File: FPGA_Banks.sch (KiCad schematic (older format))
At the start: 36 parts

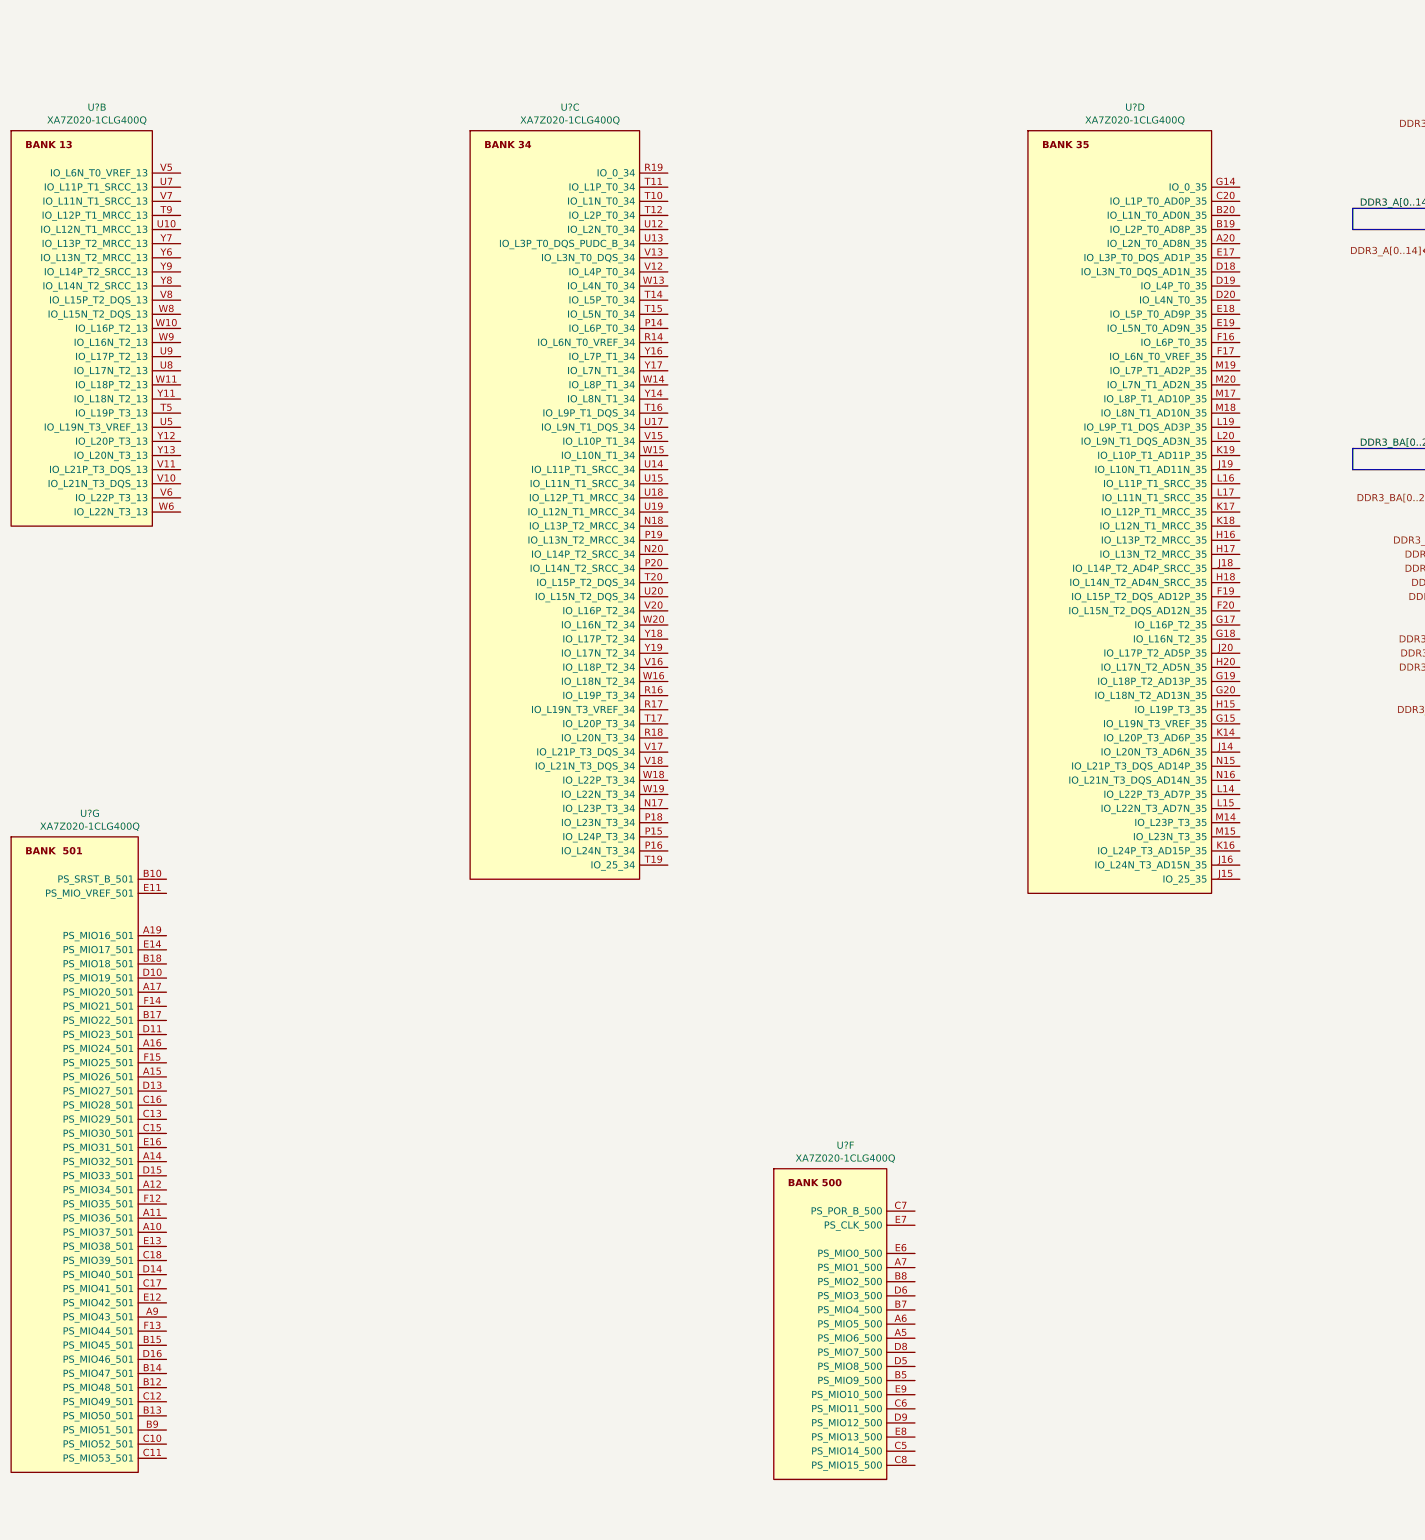
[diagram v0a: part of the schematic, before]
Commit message: Rearranged the top sheet blocks modified hir. pins in few blocks
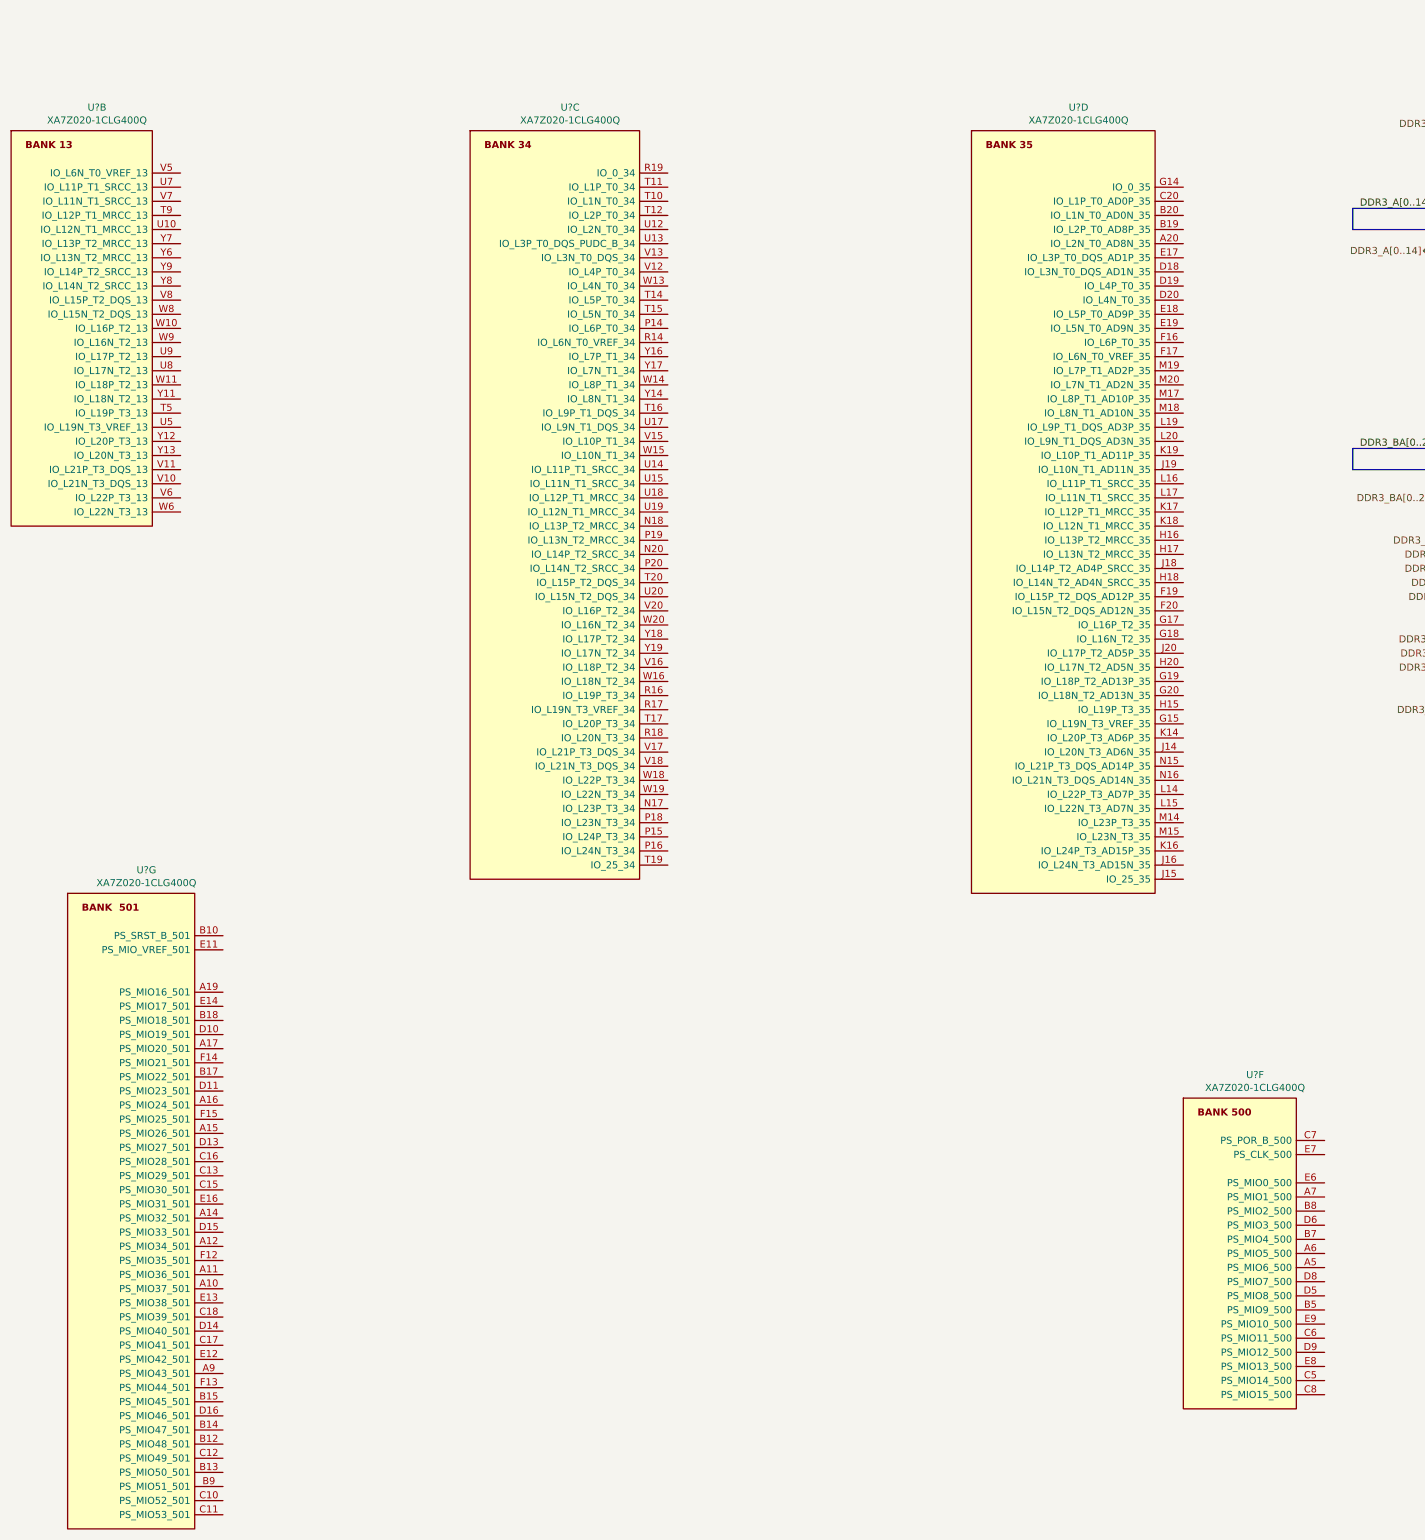
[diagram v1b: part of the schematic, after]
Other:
- moved on the sheet: U?D, U?F, U?G
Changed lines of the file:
@@
 L GM_FPGA:XA7Z020-1CLG400Q U?
 U 4 1 604A2214
-P 8200 1100
-F 0 "U?" H 8958 1265 50  0000 C CNN
-F 1 "XA7Z020-1CLG400Q" H 8958 1174 50  0000 C CNN
-F 2 "BGA400C80P20X20_1700X1700X160" H 11050 1200 50  0001 L CNN
-F 3 "http://www.xilinx.com/support/documentation/data_sheets/ds188-XA-Zynq-7000-Overview.pdf" H 11050 1100 50  0001 L CNN
-F 4 "XA7Z020-1CLG400Q" H 8200 1100 50  0001 C CNN "MPN"
-	4    8200 1100
+P 7800 1100
+F 0 "U?" H 8558 1265 50  0000 C CNN
+F 1 "XA7Z020-1CLG400Q" H 8558 1174 50  0000 C CNN
+F 2 "BGA400C80P20X20_1700X1700X160" H 10650 1200 50  0001 L CNN
+F 3 "http://www.xilinx.com/support/documentation/data_sheets/ds188-XA-Zynq-7000-Overview.pdf" H 10650 1100 50  0001 L CNN
+F 4 "XA7Z020-1CLG400Q" H 7800 1100 50  0001 C CNN "MPN"
+	4    7800 1100
 	1    0    0    -1
 $EndComp
@@
 L GM_FPGA:XA7Z020-1CLG400Q U?
 U 6 1 604B00A9
-P 6400 8450
-F 0 "U?" H 6908 8615 50  0000 C CNN
-F 1 "XA7Z020-1CLG400Q" H 6908 8524 50  0000 C CNN
-F 2 "BGA400C80P20X20_1700X1700X160" H 9250 8550 50  0001 L CNN
-F 3 "http://www.xilinx.com/support/documentation/data_sheets/ds188-XA-Zynq-7000-Overview.pdf" H 9250 8450 50  0001 L CNN
-F 4 "XA7Z020-1CLG400Q" H 6400 8450 50  0001 C CNN "MPN"
-	6    6400 8450
+P 9300 7950
+F 0 "U?" H 9808 8115 50  0000 C CNN
+F 1 "XA7Z020-1CLG400Q" H 9808 8024 50  0000 C CNN
+F 2 "BGA400C80P20X20_1700X1700X160" H 12150 8050 50  0001 L CNN
+F 3 "http://www.xilinx.com/support/documentation/data_sheets/ds188-XA-Zynq-7000-Overview.pdf" H 12150 7950 50  0001 L CNN
+F 4 "XA7Z020-1CLG400Q" H 9300 7950 50  0001 C CNN "MPN"
+	6    9300 7950
 	1    0    0    -1
 $EndComp
@@
 L GM_FPGA:XA7Z020-1CLG400Q U?
 U 7 1 604BC2A9
-P 1000 6100
-F 0 "U?" H 1558 6265 50  0000 C CNN
-F 1 "XA7Z020-1CLG400Q" H 1558 6174 50  0000 C CNN
-F 2 "BGA400C80P20X20_1700X1700X160" H 3850 6200 50  0001 L CNN
-F 3 "http://www.xilinx.com/support/documentation/data_sheets/ds188-XA-Zynq-7000-Overview.pdf" H 3850 6100 50  0001 L CNN
-F 4 "XA7Z020-1CLG400Q" H 1000 6100 50  0001 C CNN "MPN"
-	7    1000 6100
+P 1400 6500
+F 0 "U?" H 1958 6665 50  0000 C CNN
+F 1 "XA7Z020-1CLG400Q" H 1958 6574 50  0000 C CNN
+F 2 "BGA400C80P20X20_1700X1700X160" H 4250 6600 50  0001 L CNN
+F 3 "http://www.xilinx.com/support/documentation/data_sheets/ds188-XA-Zynq-7000-Overview.pdf" H 4250 6500 50  0001 L CNN
+F 4 "XA7Z020-1CLG400Q" H 1400 6500 50  0001 C CNN "MPN"
+	7    1400 6500
 	1    0    0    -1
 $EndComp

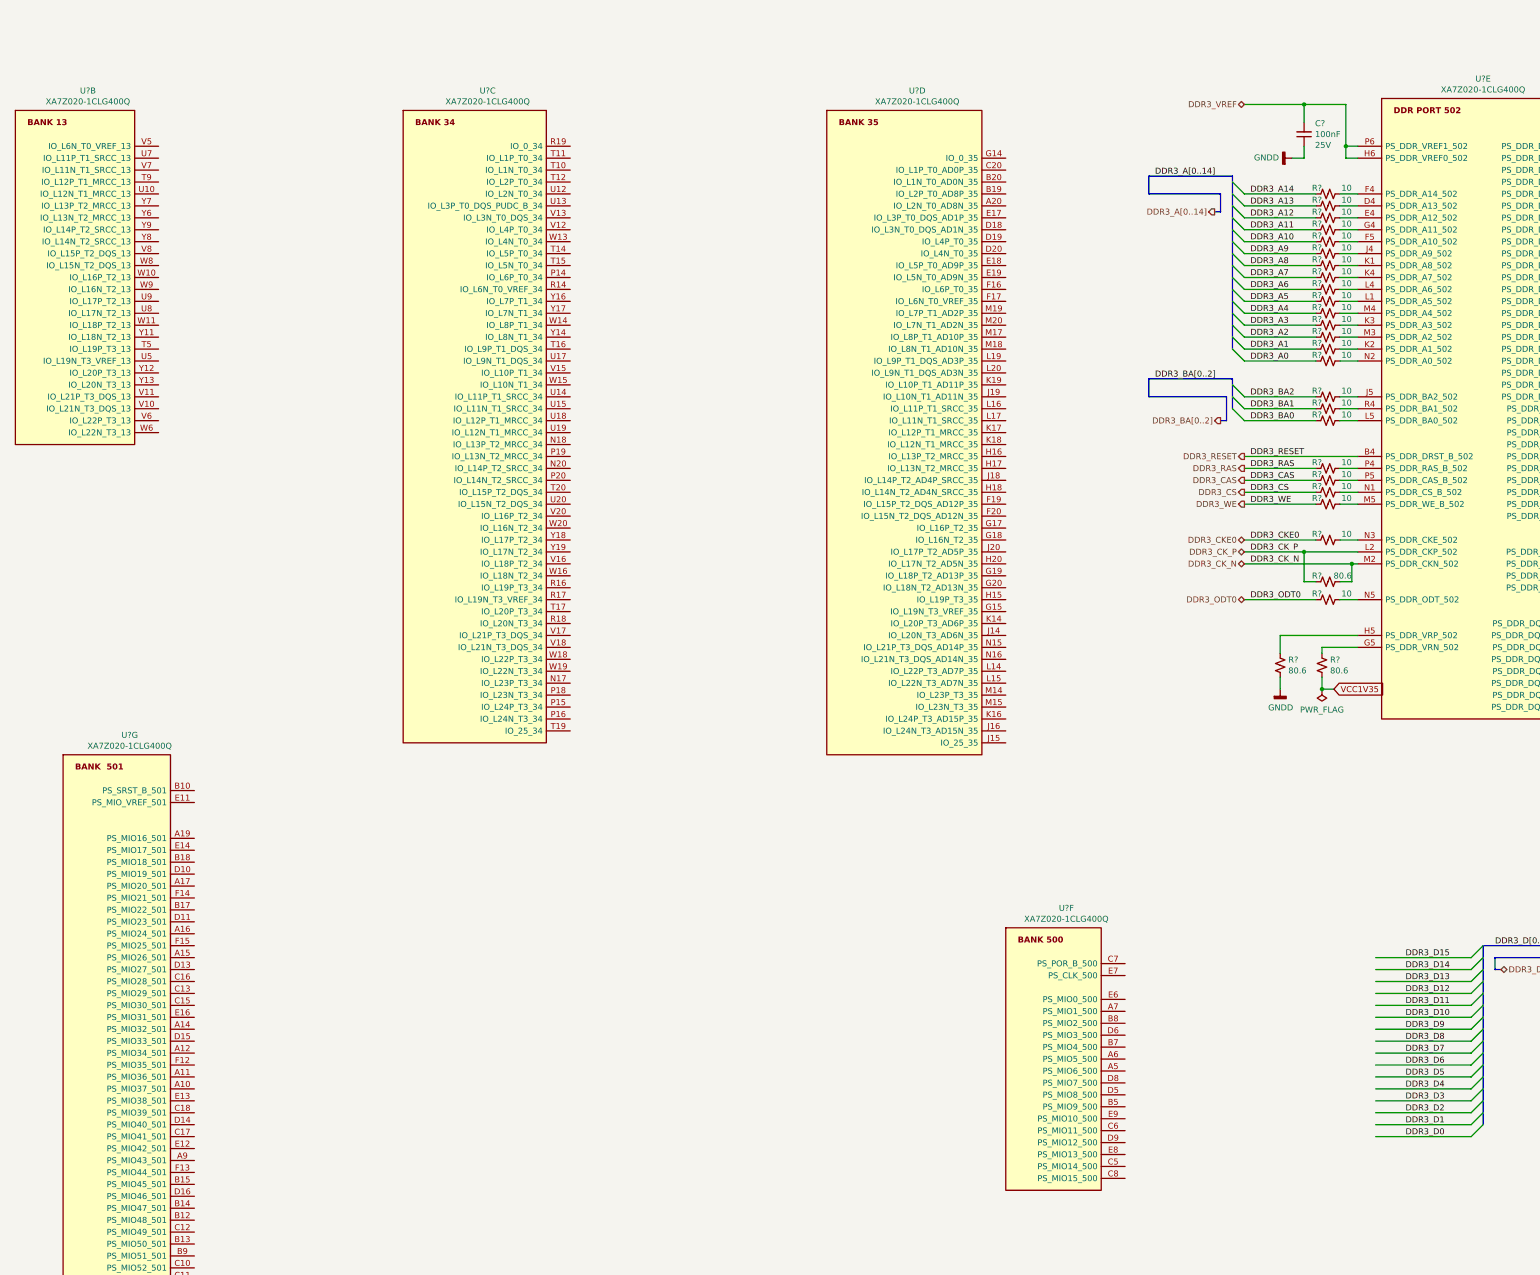
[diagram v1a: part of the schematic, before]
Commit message: Added nets for fx3 usb3 cct from fpga
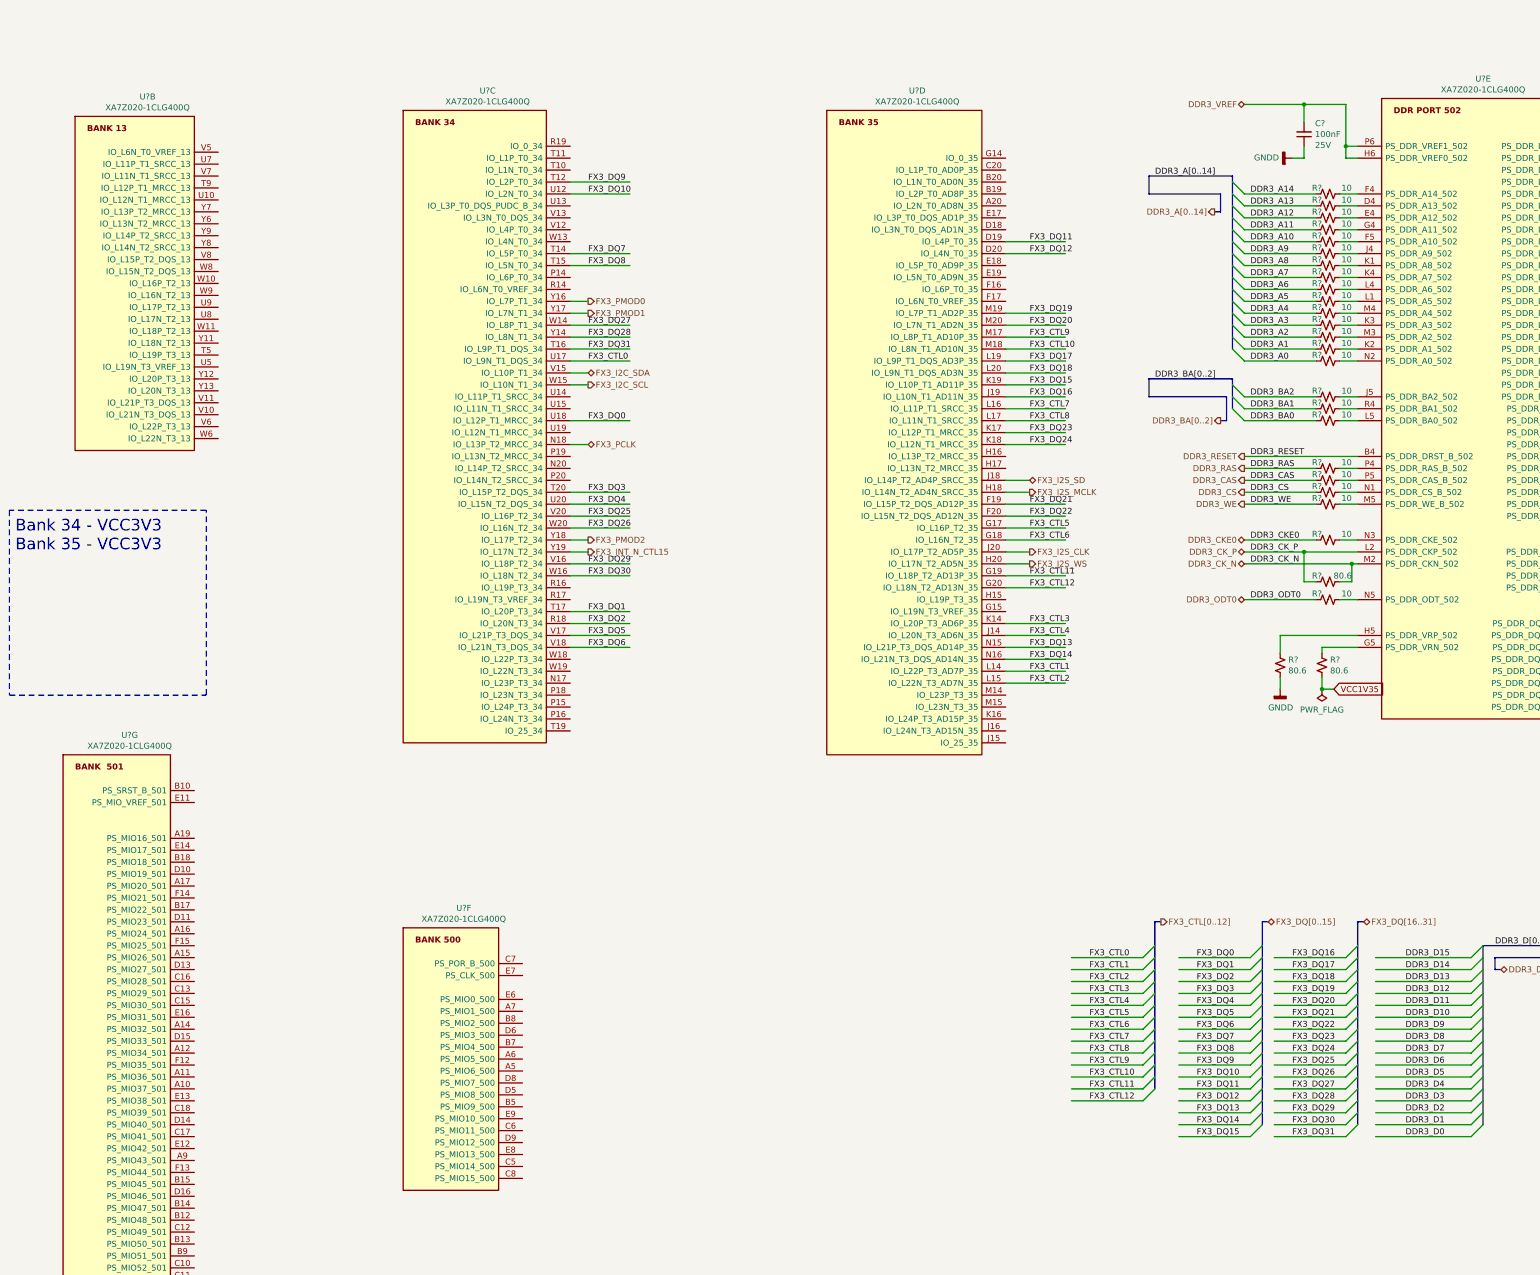
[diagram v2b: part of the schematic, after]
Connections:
- net labels added: FX3_CTL0, FX3_CTL1, FX3_CTL10, FX3_CTL11, FX3_CTL12, FX3_CTL2, FX3_CTL3, FX3_CTL4, FX3_CTL5, FX3_CTL6, FX3_CTL7, FX3_CTL8, FX3_CTL9, FX3_CTL[0..12], FX3_DQ0, FX3_DQ1, FX3_DQ10, FX3_DQ11, FX3_DQ12, FX3_DQ13, FX3_DQ14, FX3_DQ15, FX3_DQ16, FX3_DQ17, FX3_DQ18, FX3_DQ19, FX3_DQ2, FX3_DQ20, FX3_DQ21, FX3_DQ22, FX3_DQ23, FX3_DQ24, FX3_DQ25, FX3_DQ26, FX3_DQ27, FX3_DQ28, FX3_DQ29, FX3_DQ3, FX3_DQ30, FX3_DQ31, FX3_DQ4, FX3_DQ5, FX3_DQ6, FX3_DQ7, FX3_DQ8, FX3_DQ9, FX3_DQ[0..15], FX3_DQ[16..31], FX3_I2C_SCL, FX3_I2C_SDA, FX3_I2S_CLK, FX3_I2S_MCLK, FX3_I2S_SD, FX3_I2S_WS, FX3_INT_N_CTL15, FX3_PCLK, FX3_PMOD0, FX3_PMOD1, FX3_PMOD2
- wire segments 151 -> 252
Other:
- note added: "Bank 34 - VCC3V3\nBank 35 - VCC3V3"
- moved on the sheet: U?B, U?F
